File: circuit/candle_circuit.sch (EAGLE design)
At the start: 23 parts, among them IC1 TINY10P, SW1 KMR2, SW2 KMR2

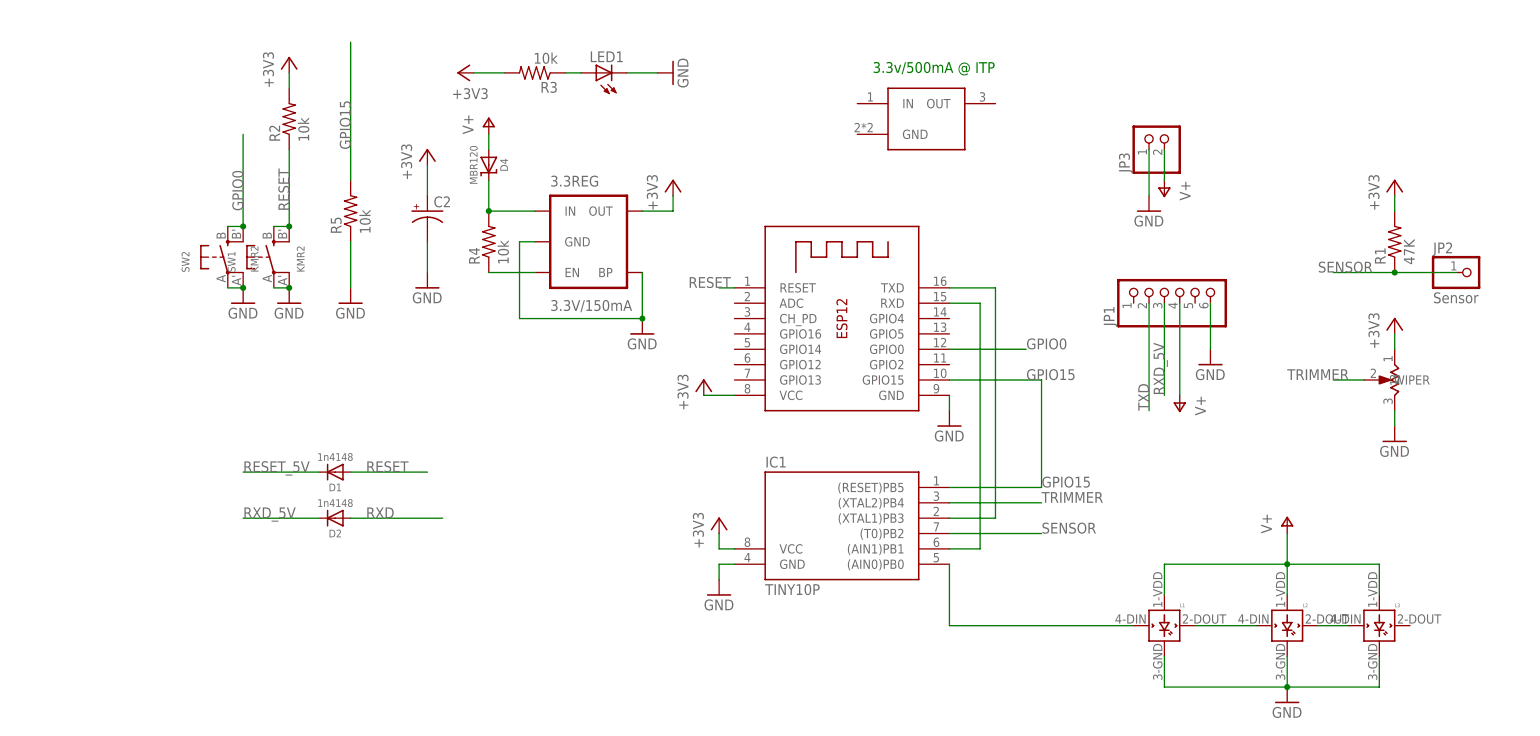
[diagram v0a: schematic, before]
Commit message: Updates to circuit, client
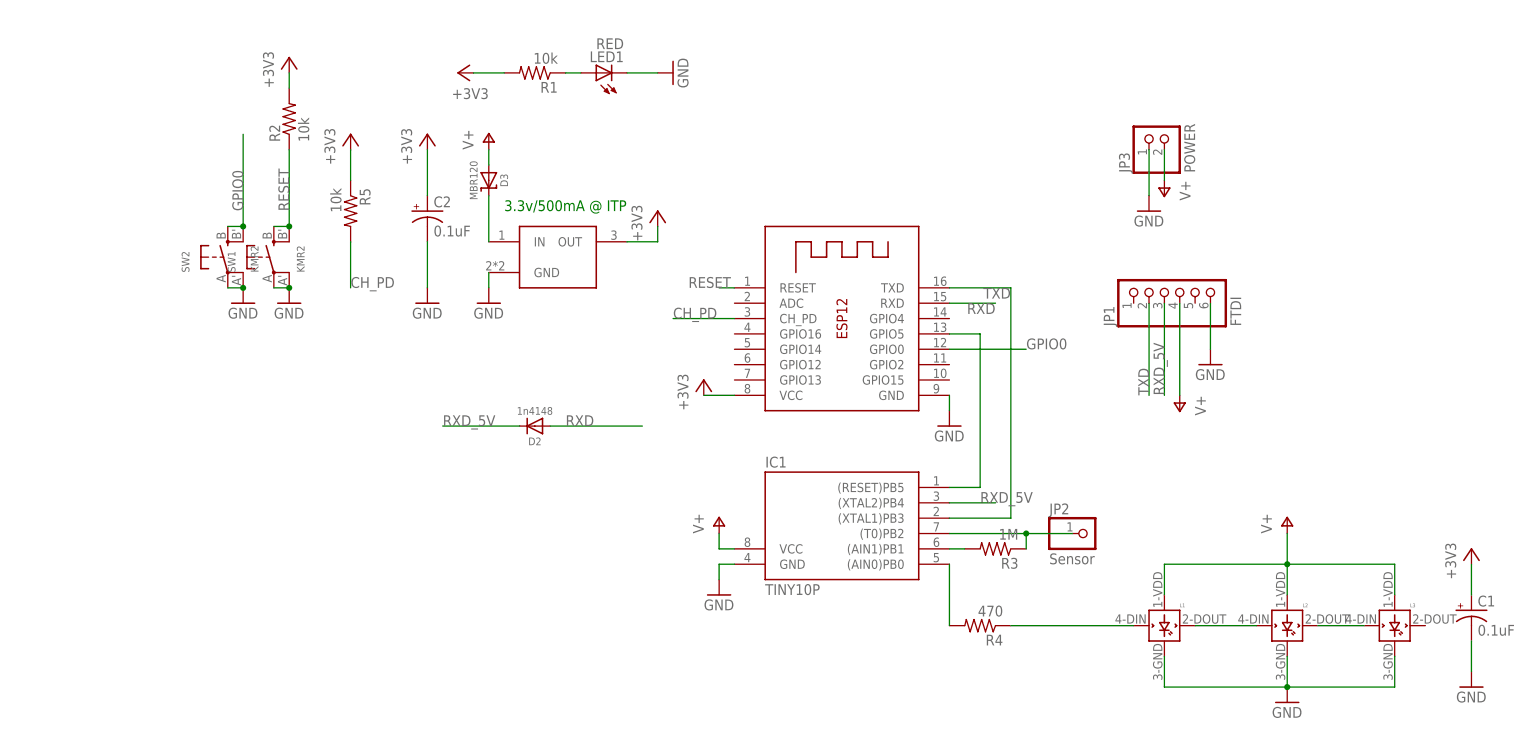
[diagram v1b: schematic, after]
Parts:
- removed 3.3REG: 3.3V/150mA, SparkFun-PowerIC:V_REG_MIC52053.3V
- removed D1: 1n4148, microbuilder:DIODESOD-323
- removed D4: MBR120, microbuilder:DIODE-SCHOTTKYSOD-123
- removed U$4: POTENTIOMETER-SMD-P3W, ITP_Lab:POTENTIOMETER-SMD-P3W
- added C1: 0.1uF, SparkFun-Capacitors:CAP_POLC
- added D3: MBR120, microbuilder:DIODE-SCHOTTKYSOD-123
- C2: value (none) -> 0.1uF
- JP1: value (none) -> FTDI
- JP3: value (none) -> POWER
- LED1: value (none) -> RED
- R1: value 47K -> 10k
- R3: value 10k -> 1M
- R4: value 10k -> 470
- X1: value (none) -> ESP-12
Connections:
- removed net N$10: 3.3REG.IN, D4.C, R4.2
- removed net N$9: 3.3REG.EN, R4.1
- removed net RESET_5V: D1.C
- removed net TRIMMER: IC1.(XTAL2)PB4, U$4.WIPER
- new net CH_PD: R5.2, X1.CH_PD
- new net N$5: D3.C, U$1.IN
- new net N$7: IC1.(AIN1)PB1, R3.2
- new net N$8: L1.DIN, R4.1
- net +3V3: now also C1.+, R5.1, U$1.OUT; no longer 3.3REG.OUT, IC1.VCC, R3.2, U$4.1
- net GND: now also C1.-, U$1.GND; no longer 3.3REG.BP, 3.3REG.GND, R5.1, U$4.3
- net GPIO15: now also X1.GPIO5; no longer R5.2, X1.GPIO15
- net N$1: now also R4.2; no longer L1.DIN
- net N$4: now also R1.1; no longer R3.1
- net RESET: no longer D1.A
- net RXD: no longer IC1.(AIN1)PB1
- net RXD_5V: now also IC1.(XTAL2)PB4
- net SENSOR: now also R3.1; no longer R1.1
- net V+: now also D3.A, IC1.VCC; no longer D4.A
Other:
- moved on the sheet: D2, JP2, L3, R1, R3, R4, R5

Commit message: Circuit board updates
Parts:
- added R7, R8: 10K, microbuilder:RESISTOR0805_NOOUTLINE
- LED1: device adafruit:LEDCHIPLED_0603 -> microbuilder:LED0805_NOOUTLINE
- R1: value 10k -> 1k
- R3: value 1M -> 10k
- R5: value 10k -> 1M
- renumbered D3 to D1, R4 to R6
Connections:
- new net GPIO2: R8.1, X1.GPIO2
- new net N$6: LED1.C, R1.1
- net +3V3: now also LED1.A, R3.1, R8.2; no longer R1.2, R5.1
- net CH_PD: now also R3.2; no longer R5.2
- net GND: now also R7.1; no longer LED1.C
- net GPIO0: now also R1.2
- net GPIO15: now also R7.2, X1.GPIO15; no longer IC1.(RESET)PB5, X1.GPIO5
- net N$4: now also IC1.(RESET)PB5, X1.GPIO5; no longer LED1.A, R1.1
- net N$7: now also R5.2; no longer R3.2
- net SENSOR: now also R5.1; no longer R3.1
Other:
- moved on the sheet: C1, C2, R1, R3, R5

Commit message: board update
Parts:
- removed R8: 10K, microbuilder:RESISTOR0805_NOOUTLINE
- added JP4, JP5: Test, microbuilder:HEADER-1X2
- added R4: 10k, adafruit:R-US_R0603
- R5: value 1M -> 10k
- R6: value 470 -> 1M
- R7: value 10K -> 470; device microbuilder:RESISTOR0805_NOOUTLINE -> adafruit:R-US_R0603
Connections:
- net +3V3: now also JP5.2, R4.1; no longer R8.2
- net GND: now also JP4.1, JP5.1, R5.2; no longer R7.1
- net GPIO15: now also R5.1; no longer R7.2
- net GPIO2: now also R4.2; no longer R8.1
- net N$1: now also R7.2; no longer R6.2
- net N$7: now also R6.2; no longer R5.2
- net N$8: now also R7.1; no longer R6.1
- net SENSOR: now also R6.1; no longer R5.1
- net V+: now also JP4.2
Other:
- moved on the sheet: C1, D1, R5, R6

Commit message: Board updates
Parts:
- JP5: value Test -> TEST; device microbuilder:HEADER-1X2 -> pinhead:PINHD-1X1
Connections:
- net +3V3: now also JP5.1; no longer JP5.2
- net GND: no longer JP5.1
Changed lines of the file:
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@@
 <part name="R4" library="adafruit" deviceset="R-US_" device="R0603" value="10k"/>
 <part name="JP4" library="microbuilder" deviceset="HEADER-1X2" device="" value="Test"/>
-<part name="JP5" library="microbuilder" deviceset="HEADER-1X2" device="" value="Test"/>
 <part name="GND8" library="supply1" deviceset="GND" device=""/>
-<part name="GND12" library="supply1" deviceset="GND" device=""/>
 <part name="P+4" library="supply1" deviceset="V+" device=""/>
+<part name="JP5" library="pinhead" deviceset="PINHD-1X1" device="" value="TEST"/>
 <part name="+3V8" library="supply1" deviceset="+3V3" device=""/>
 </parts>
@@
 <instance part="R4" gate="G$1" x="-40.64" y="81.28" rot="R270"/>
 <instance part="JP4" gate="G$1" x="101.6" y="93.98" rot="R90"/>
-<instance part="JP5" gate="G$1" x="119.38" y="93.98" rot="R90"/>
 <instance part="GND8" gate="1" x="99.06" y="81.28"/>
-<instance part="GND12" gate="1" x="116.84" y="78.74"/>
 <instance part="P+4" gate="1" x="101.6" y="83.82" rot="R180"/>
-<instance part="+3V8" gate="G$1" x="119.38" y="81.28" rot="R180"/>
+<instance part="JP5" gate="G$1" x="114.3" y="93.98" rot="R90"/>
+<instance part="+3V8" gate="G$1" x="114.3" y="81.28" rot="R180"/>
 </instances>
 <busses>
@@
 <wire x1="99.06" y1="91.44" x2="99.06" y2="83.82" width="0.1524" layer="91"/>
 </segment>
-<segment>
-<pinref part="JP5" gate="G$1" pin="1"/>
-<pinref part="GND12" gate="1" pin="GND"/>
-<wire x1="116.84" y1="91.44" x2="116.84" y2="81.28" width="0.1524" layer="91"/>
-</segment>
 </net>
 <net name="+3V3" class="0">
@@
 </segment>
 <segment>
-<pinref part="JP5" gate="G$1" pin="2"/>
+<pinref part="JP5" gate="G$1" pin="1"/>
 <pinref part="+3V8" gate="G$1" pin="+3V3"/>
-<wire x1="119.38" y1="91.44" x2="119.38" y2="83.82" width="0.1524" layer="91"/>
+<wire x1="114.3" y1="91.44" x2="114.3" y2="83.82" width="0.1524" layer="91"/>
 </segment>
 </net>

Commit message: Updates to board and schematic
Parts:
- JP1: value FTDI -> Serial
- JP4: value Test -> V+ Test
- JP5: value TEST -> 3V3 Test
- renumbered U$1 to U1, X1 to IC2
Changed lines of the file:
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@@
 </classes>
 <parts>
-<part name="X1" library="adafruit" deviceset="ESP-12" device="" value="ESP-12"/>
+<part name="IC2" library="adafruit" deviceset="ESP-12" device="" value="ESP-12"/>
 <part name="IC1" library="atmel" deviceset="TINY10" device="P"/>
 <part name="+3V1" library="supply1" deviceset="+3V3" device=""/>
@@
 <part name="P+2" library="supply1" deviceset="V+" device=""/>
 <part name="JP2" library="pinhead" deviceset="PINHD-1X1" device="" value="Sensor"/>
-<part name="U$1" library="ITP_Lab" deviceset="REGULATOR" device="3.3V-UA78M33CDCYR"/>
+<part name="U1" library="ITP_Lab" deviceset="REGULATOR" device="3.3V-UA78M33CDCYR"/>
 <part name="C1" library="SparkFun-Capacitors" deviceset="CAP_POL" device="C" value="0.1uF"/>
 <part name="R2" library="adafruit" deviceset="R-US_" device="R0603" value="10k"/>
 <part name="JP3" library="microbuilder" deviceset="HEADER-1X2" device="" value="POWER"/>
 <part name="GND11" library="supply1" deviceset="GND" device=""/>
-<part name="JP1" library="microbuilder" deviceset="HEADER-1X6" device="" value="FTDI"/>
+<part name="JP1" library="microbuilder" deviceset="HEADER-1X6" device="" value="Serial"/>
 <part name="+3V9" library="supply1" deviceset="+3V3" device=""/>
 <part name="GND13" library="supply1" deviceset="GND" device=""/>
@@
 <part name="R5" library="adafruit" deviceset="R-US_" device="R0603" value="10k"/>
 <part name="R4" library="adafruit" deviceset="R-US_" device="R0603" value="10k"/>
-<part name="JP4" library="microbuilder" deviceset="HEADER-1X2" device="" value="Test"/>
+<part name="JP4" library="microbuilder" deviceset="HEADER-1X2" device="" value="V+ Test"/>
 <part name="GND8" library="supply1" deviceset="GND" device=""/>
 <part name="P+4" library="supply1" deviceset="V+" device=""/>
-<part name="JP5" library="pinhead" deviceset="PINHD-1X1" device="" value="TEST"/>
+<part name="JP5" library="pinhead" deviceset="PINHD-1X1" device="" value="3V3 Test"/>
 <part name="+3V8" library="supply1" deviceset="+3V3" device=""/>
 </parts>
@@
 </plain>
 <instances>
-<instance part="X1" gate="G$1" x="30.48" y="63.5"/>
+<instance part="IC2" gate="G$1" x="30.48" y="63.5"/>
 <instance part="IC1" gate="G$1" x="30.48" y="27.94"/>
 <instance part="+3V1" gate="G$1" x="7.62" y="53.34"/>
@@
 <instance part="P+2" gate="1" x="86.36" y="48.26" rot="R180"/>
 <instance part="JP2" gate="G$1" x="71.12" y="27.94"/>
-<instance part="U$1" gate="G$1" x="2.54" y="93.98"/>
+<instance part="U1" gate="G$1" x="2.54" y="93.98"/>
 <instance part="C1" gate="G$1" x="-17.78" y="99.06"/>
 <instance part="R2" gate="G$1" x="-60.96" y="96.52" rot="R90"/>
@@
 </segment>
 <segment>
-<pinref part="X1" gate="G$1" pin="GND"/>
+<pinref part="IC2" gate="G$1" pin="GND"/>
 <pinref part="GND3" gate="1" pin="GND"/>
 <wire x1="48.26" y1="50.8" x2="48.26" y2="48.26" width="0.1524" layer="91"/>
@@
 <segment>
 <pinref part="GND13" gate="1" pin="GND"/>
-<pinref part="U$1" gate="G$1" pin="GND"/>
+<pinref part="U1" gate="G$1" pin="GND"/>
 <wire x1="-7.62" y1="86.36" x2="-7.62" y2="88.9" width="0.1524" layer="91"/>
 </segment>
@@
 <net name="+3V3" class="0">
 <segment>
-<pinref part="X1" gate="G$1" pin="VCC"/>
+<pinref part="IC2" gate="G$1" pin="VCC"/>
 <pinref part="+3V1" gate="G$1" pin="+3V3"/>
 <wire x1="12.7" y1="50.8" x2="7.62" y2="50.8" width="0.1524" layer="91"/>
@@
 <pinref part="+3V9" gate="G$1" pin="+3V3"/>
 <wire x1="20.32" y1="96.52" x2="20.32" y2="93.98" width="0.1524" layer="91"/>
-<pinref part="U$1" gate="G$1" pin="OUT"/>
+<pinref part="U1" gate="G$1" pin="OUT"/>
 <wire x1="20.32" y1="93.98" x2="15.24" y2="93.98" width="0.1524" layer="91"/>
 </segment>
@@
 </segment>
 <segment>
-<pinref part="X1" gate="G$1" pin="RESET"/>
+<pinref part="IC2" gate="G$1" pin="RESET"/>
 <wire x1="12.7" y1="68.58" x2="10.16" y2="68.58" width="0.1524" layer="91"/>
 <label x="5.08" y="68.58" size="1.778" layer="95"/>
@@
 <net name="GPIO15" class="0">
 <segment>
-<pinref part="X1" gate="G$1" pin="GPIO15"/>
+<pinref part="IC2" gate="G$1" pin="GPIO15"/>
 <wire x1="48.26" y1="53.34" x2="60.96" y2="53.34" width="0.1524" layer="91"/>
 <label x="60.96" y="53.34" size="1.778" layer="95"/>
@@
 </segment>
 <segment>
-<pinref part="X1" gate="G$1" pin="GPIO0"/>
+<pinref part="IC2" gate="G$1" pin="GPIO0"/>
 <wire x1="48.26" y1="58.42" x2="60.96" y2="58.42" width="0.1524" layer="91"/>
 <label x="60.96" y="58.42" size="1.778" layer="95"/>
@@
 </segment>
 <segment>
-<pinref part="X1" gate="G$1" pin="RXD"/>
+<pinref part="IC2" gate="G$1" pin="RXD"/>
 <wire x1="48.26" y1="66.04" x2="55.88" y2="66.04" width="0.1524" layer="91"/>
 <label x="55.88" y="66.04" size="1.778" layer="95" rot="R180"/>
@@
 <wire x1="48.26" y1="30.48" x2="58.42" y2="30.48" width="0.1524" layer="91"/>
 <wire x1="58.42" y1="30.48" x2="58.42" y2="68.58" width="0.1524" layer="91"/>
-<pinref part="X1" gate="G$1" pin="TXD"/>
+<pinref part="IC2" gate="G$1" pin="TXD"/>
 <wire x1="58.42" y1="68.58" x2="48.26" y2="68.58" width="0.1524" layer="91"/>
 <label x="58.42" y="68.58" size="1.778" layer="95" rot="R180"/>
@@
 <segment>
 <pinref part="D1" gate="G$1" pin="C"/>
-<pinref part="U$1" gate="G$1" pin="IN"/>
+<pinref part="U1" gate="G$1" pin="IN"/>
 <wire x1="-7.62" y1="101.6" x2="-7.62" y2="93.98" width="0.1524" layer="91"/>
 </segment>
@@
 <net name="CH_PD" class="0">
 <segment>
-<pinref part="X1" gate="G$1" pin="CH_PD"/>
+<pinref part="IC2" gate="G$1" pin="CH_PD"/>
 <wire x1="12.7" y1="63.5" x2="2.54" y2="63.5" width="0.1524" layer="91"/>
 <label x="2.54" y="63.5" size="1.778" layer="95"/>
@@
 <net name="GPIO2" class="0">
 <segment>
-<pinref part="X1" gate="G$1" pin="GPIO2"/>
+<pinref part="IC2" gate="G$1" pin="GPIO2"/>
 <wire x1="48.26" y1="55.88" x2="60.96" y2="55.88" width="0.1524" layer="91"/>
 <label x="60.96" y="55.88" size="1.778" layer="95"/>
@@
 <wire x1="48.26" y1="35.56" x2="53.34" y2="35.56" width="0.1524" layer="91"/>
 <wire x1="53.34" y1="35.56" x2="53.34" y2="60.96" width="0.1524" layer="91"/>
-<pinref part="X1" gate="G$1" pin="GPIO5"/>
+<pinref part="IC2" gate="G$1" pin="GPIO5"/>
 <wire x1="53.34" y1="60.96" x2="48.26" y2="60.96" width="0.1524" layer="91"/>
 </segment>
